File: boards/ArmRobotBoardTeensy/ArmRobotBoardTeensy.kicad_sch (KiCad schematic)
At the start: 49 parts, among them J1 B5B-XH-A, J10 B4B-XH-A, J11 B3B-XH-A, J2 B4B-XH-A, J3 B3B-XH-A, J4 B3B-XH-A, J5 B4B-XH-A, J6 B2B-XH-A, J7 B2B-XH-A, J8 B4B-XH-A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

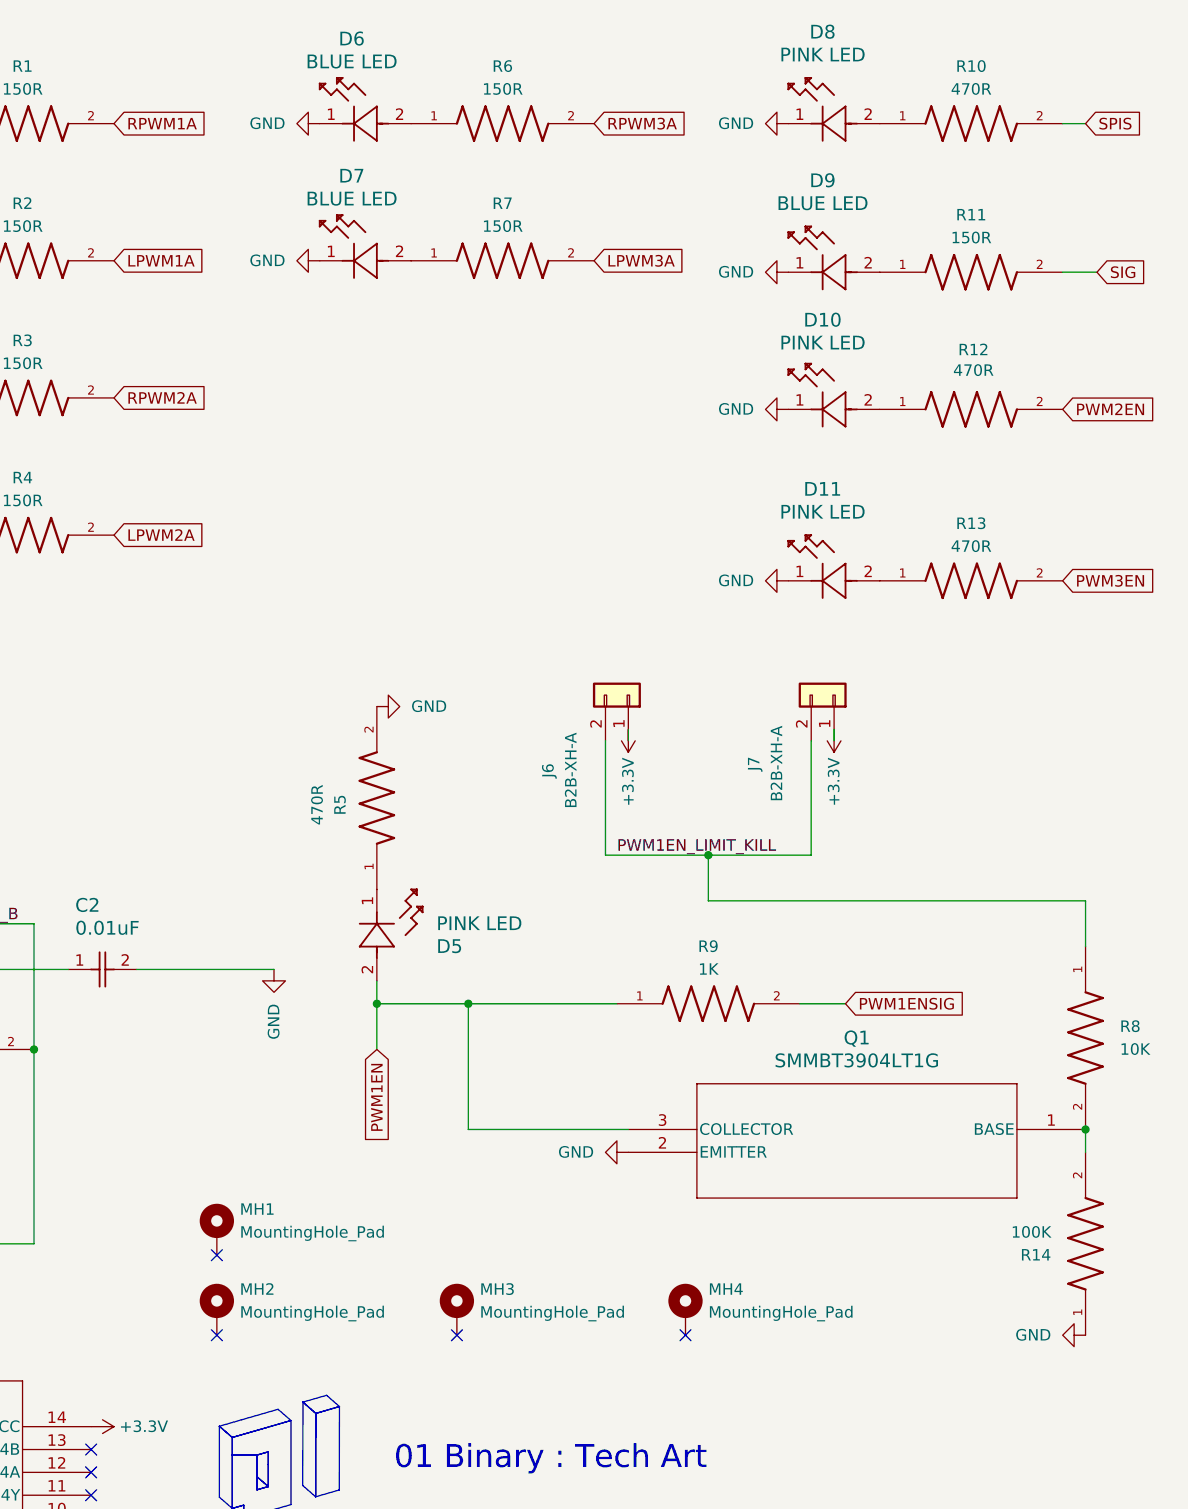
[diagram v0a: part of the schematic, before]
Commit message: Fix hi-z (floating) pins for solenoid and PWM channel 1
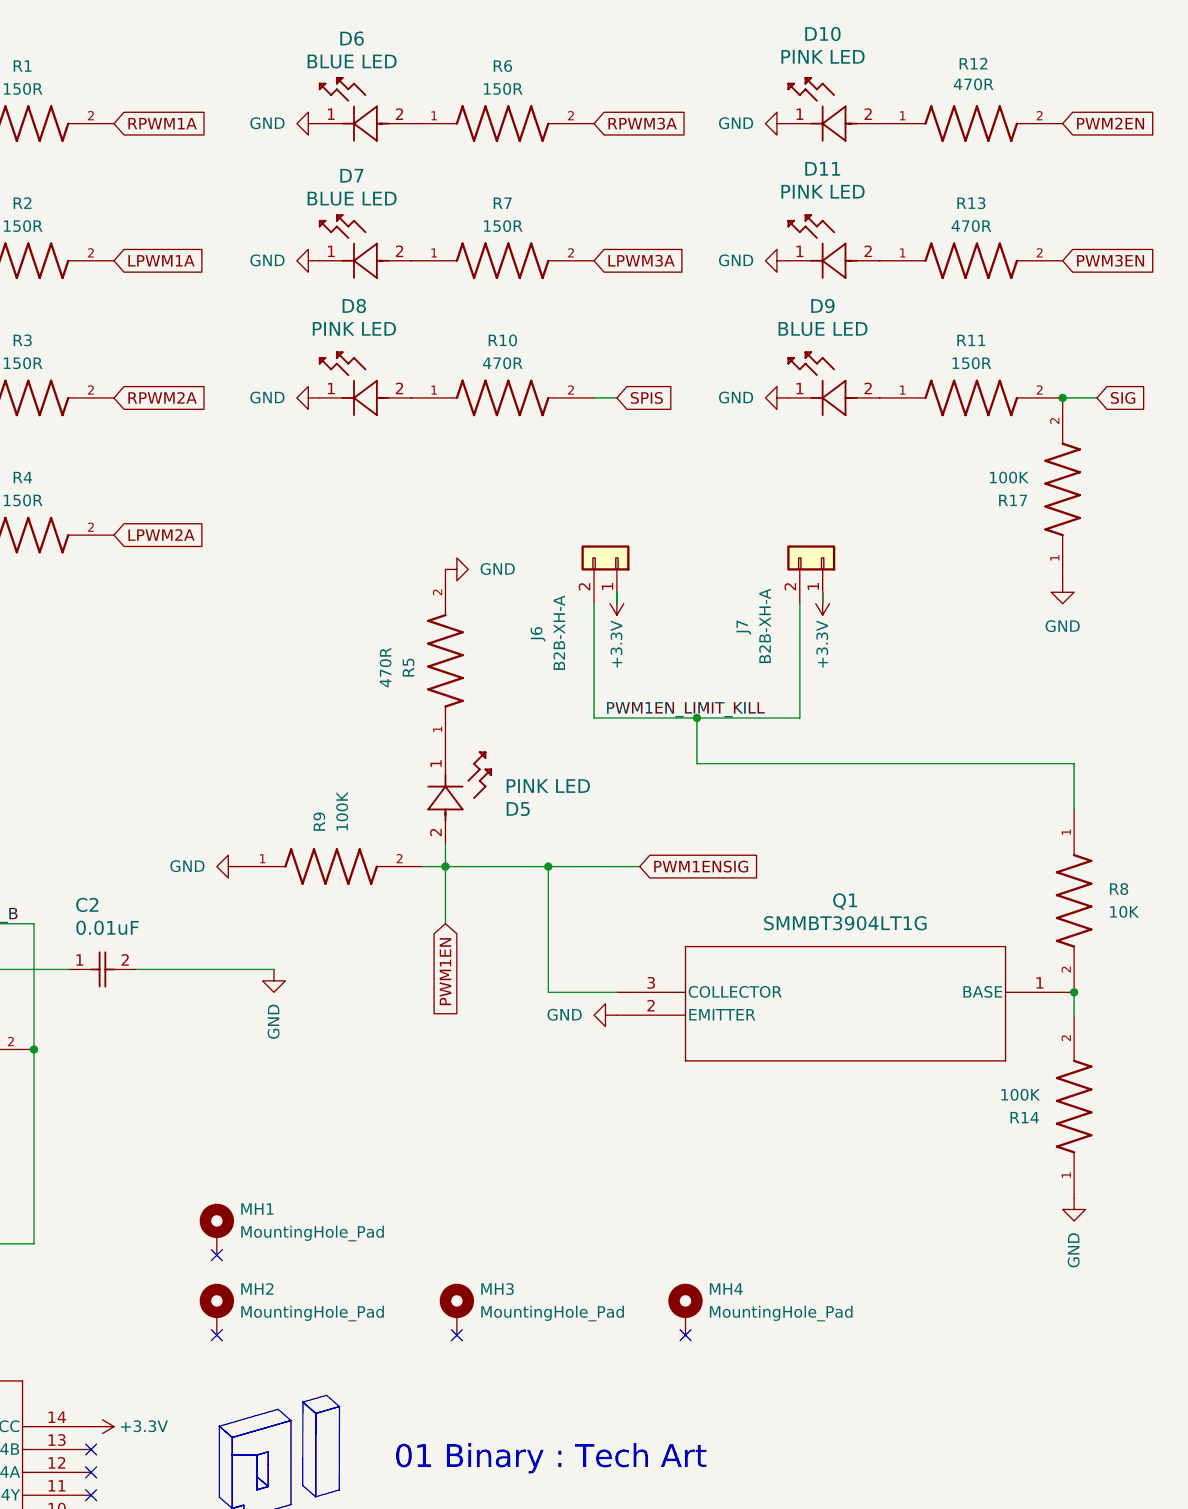
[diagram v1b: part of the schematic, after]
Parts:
- removed R9: 1K, RCG06031K00FKEA:RCG06031K00FKEA, symbol RCG06031K00FKEA:RCG06031K00FKEA
- added R17, R9: 100K, CRCW0603100KFKEA:CRCW0603100KFKEA, symbol CRCW0603100KFKEA:CRCW0603100KFKEA
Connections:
- net PWM1ENSIG is gone; now on net PWM1EN: U1.2 (0_RX1_CRX2_CS1)
- net GND: now also R17.1, R9.1
- net PWM1EN: now also R9.2
- net SIG: now also R17.2
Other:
- moved on the sheet: D10, D11, D5, D8, D9, J6, J7, Q1, R10, R11, R12, R13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

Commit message: Clean up and document boards
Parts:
- added R18, R19, R20: 5.1K, RC0603FR-075K1L:RC0603FR-075K1L, symbol RCG06031K00FKEA:RCG06031K00FKEA
- D10, D11, D5, D8: value PINK LED -> RED LED; footprint XL-2012UPC:LED_XL-2012SURC_XLG -> NCD0603R1:NCD0603R1; LCSC C965812 -> C84263
- R10, R12, R13, R5: value 470R -> 1K; footprint RC0603FR-07470RL:RC0603FR-07470RL -> RCG06031K00FKEA:RCG06031K00FKEA; LCSC C114669 -> C4264491
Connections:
- net GND: now also R18.2, R19.2, R20.2
- net PWM1VT: now also R18.1
- net PWM2VT: now also R19.1
- net PWM3VT: now also R20.1
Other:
- moved on the sheet: C1, C2, D10, D6, D7, J1, J10, J11, J2, J3, J4, J5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
